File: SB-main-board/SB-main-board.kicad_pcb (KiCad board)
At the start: 4 copper layers, 53 x 40 mm, 98 parts, among them J1 XT30PB_IN, J2 USB_C_Receptacle_USB2.0_16P, J3 Excluder, J4 PT100, J5 Hotend, J6 FAN2, J7 LDC, J8 FS, J9 FAN, Q1 BUK9M8R5-40EX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

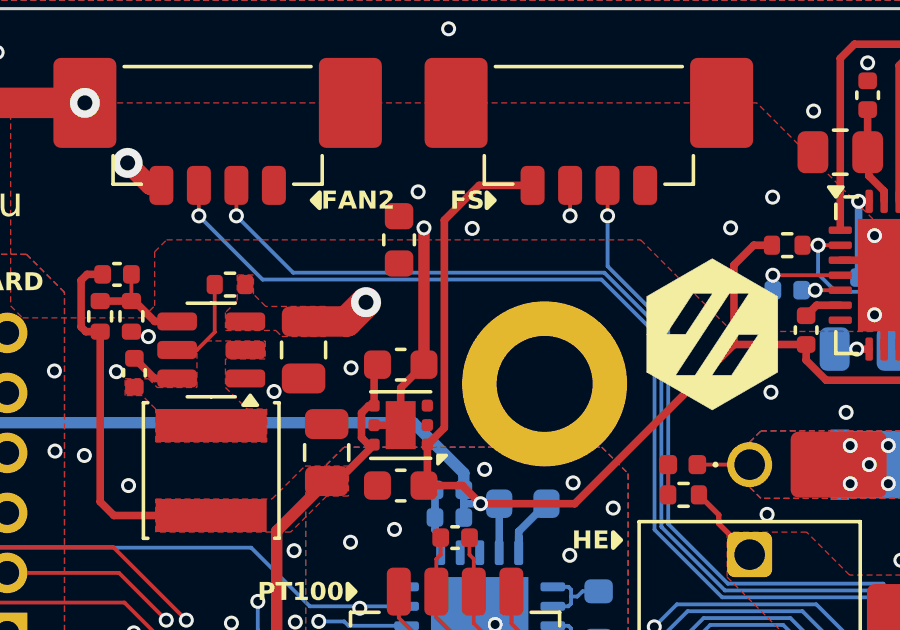
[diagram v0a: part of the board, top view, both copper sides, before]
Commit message: silkscreen: make silkscreen easy to read
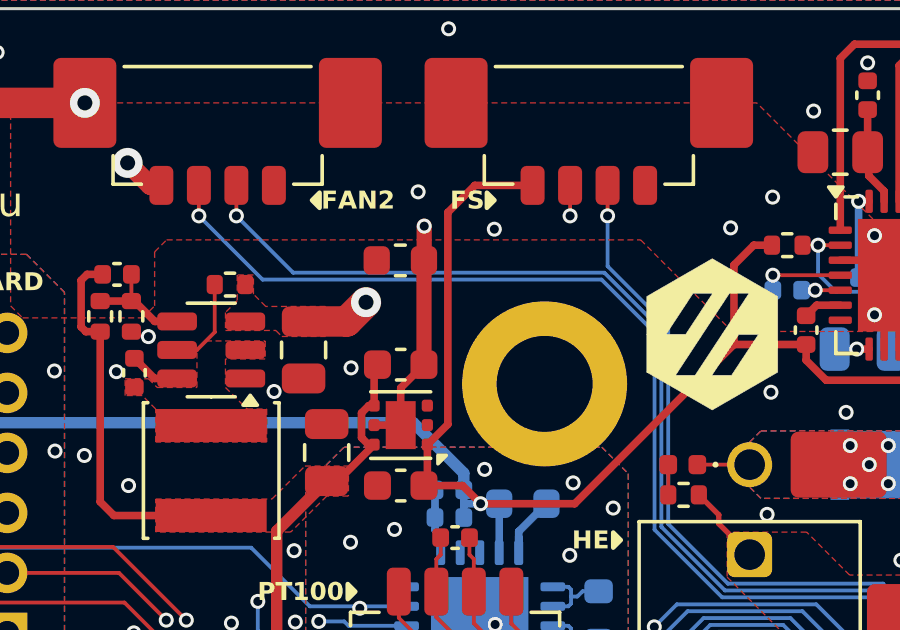
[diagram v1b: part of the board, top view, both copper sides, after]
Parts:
- moved FB4 0.69 mm to (93.3, 76.0), turned to 180 degrees
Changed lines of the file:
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@@
 	(footprint "Inductor_SMD:L_0603_1608Metric"
 		(layer "F.Cu")
-		(at 93.21893 75.305064 -90)
+		(at 93.261329 75.990864 180)
 		(descr "Inductor SMD 0603 (1608 Metric), square (rectangular) end terminal, IPC_7351 nominal, (Body size source: http://www.tortai-tech.com/upload/download/2011102023233369053.pdf), generated with kicad-footprint-generator")
 		(tags "inductor")
 		(property "Reference" "FB4"
-			(at 0 -1.43 90)
+			(at 0 -1.43 360)
 			(layer "F.SilkS")
 			(hide yes)
@@
 		)
 		(property "Value" "120R@100MHz"
-			(at 0 1.43 90)
+			(at 0 1.43 360)
 			(layer "F.Fab")
 			(hide yes)
@@
 		)
 		(property "Footprint" "Inductor_SMD:L_0603_1608Metric"
-			(at 0 0 -90)
+			(at 0 0 180)
 			(unlocked yes)
 			(layer "F.Fab")
@@
 		)
 		(property "Datasheet" ""
-			(at 0 0 -90)
+			(at 0 0 180)
 			(unlocked yes)
 			(layer "F.Fab")
@@
 		)
 		(property "Description" "Ferrite bead"
-			(at 0 0 -90)
+			(at 0 0 180)
 			(unlocked yes)
 			(layer "F.Fab")
@@
 		)
 		(fp_line
-			(start -1.48 0.73)
-			(end -1.48 -0.73)
+			(start 1.48 0.73)
+			(end -1.48 0.73)
 			(stroke
 				(width 0.05)
@@
 		)
 		(fp_line
-			(start 1.48 0.73)
-			(end -1.48 0.73)
+			(start 1.48 -0.73)
+			(end 1.48 0.73)
 			(stroke
 				(width 0.05)
@@
 		)
 		(fp_line
-			(start -1.48 -0.73)
-			(end 1.48 -0.73)
+			(start -1.48 0.73)
+			(end -1.48 -0.73)
 			(stroke
 				(width 0.05)
@@
 		)
 		(fp_line
-			(start 1.48 -0.73)
-			(end 1.48 0.73)
+			(start -1.48 -0.73)
+			(end 1.48 -0.73)
 			(stroke
 				(width 0.05)
@@
 		)
 		(fp_line
-			(start -0.8 0.4)
-			(end -0.8 -0.4)
+			(start 0.8 0.4)
+			(end -0.8 0.4)
 			(stroke
 				(width 0.1)
@@
 		)
 		(fp_line
-			(start 0.8 0.4)
-			(end -0.8 0.4)
+			(start 0.8 -0.4)
+			(end 0.8 0.4)
 			(stroke
 				(width 0.1)
@@
 		)
 		(fp_line
-			(start -0.8 -0.4)
-			(end 0.8 -0.4)
+			(start -0.8 0.4)
+			(end -0.8 -0.4)
 			(stroke
 				(width 0.1)
@@
 		)
 		(fp_line
-			(start 0.8 -0.4)
-			(end 0.8 0.4)
+			(start -0.8 -0.4)
+			(end 0.8 -0.4)
 			(stroke
 				(width 0.1)
@@
 		)
 		(fp_text user "${REFERENCE}"
-			(at 0 0 90)
+			(at 0 0 360)
 			(layer "F.Fab")
 			(effects
@@
 		)
 		(pad "1" smd roundrect
-			(at -0.787501 0 270)
+			(at -0.787501 0 180)
 			(size 0.875 0.95)
 			(layers "F.Cu" "F.Paste" "F.Mask")
@@
 		)
 		(pad "2" smd roundrect
-			(at 0.787501 0 270)
+			(at 0.787501 0 180)
 			(size 0.875 0.95)
 			(layers "F.Cu" "F.Paste" "F.Mask")
@@
 		)
 		(height 4.487268)
-		(gr_text "40.0000 mm"
+		(gr_text "1574.8031 mils"
 			(at 127.27033 87.598664 90)
 			(layer "F.Fab")
@@
 		)
 		(height -3.126866)
-		(gr_text "53.0000 mm"
+		(gr_text "2086.6139 mils"
 			(at 98.906924 64.795664 0)
 			(layer "F.Fab")
@@
 	)
 	(segment
+		(start 94.05713 75.982564)
+		(end 94.04883 75.990864)
+		(width 0.381)
+		(layer "F.Cu")
+		(net 2)
+	)
+	(segment
+		(start 94.04883 74.856164)
+		(end 94.05713 74.847864)
+		(width 0.381)
+		(layer "F.Cu")
+		(net 2)
+	)
+	(segment
 		(start 111.387722 78.946165)
 		(end 111.387722 77.483665)
@@
 	)
 	(segment
-		(start 94.04883 74.905664)
-		(end 94.04883 79.465664)
-		(width 0.381)
+		(start 94.05713 74.847864)
+		(end 94.05713 75.982564)
+		(width 0.508)
 		(layer "F.Cu")
 		(net 2)
@@
 	)
 	(segment
+		(start 94.04883 79.465664)
+		(end 94.04883 75.990864)
+		(width 0.508)
+		(layer "F.Cu")
+		(net 2)
+	)
+	(segment
 		(start 109.887722 75.983665)
 		(end 110.387722 76.483665)
@@
 	)
 	(via
-		(at 95.65733 74.924064)
+		(at 96.39393 74.949464)
 		(size 0.5)
 		(drill 0.3)
@@
 	)
 	(via
-		(at 94.04883 74.905664)
+		(at 94.05713 74.847864)
 		(size 0.5)
 		(drill 0.3)
@@
 	)
 	(segment
-		(start 94.16133 82.130664)
-		(end 94.1698 82.130664)
+		(start 94.84453 81.455934)
+		(end 94.84453 74.390664)
 		(width 0.254)
 		(layer "F.Cu")
@@
 	)
 	(segment
-		(start 94.72743 74.648564)
-		(end 95.88633 73.489664)
+		(start 94.16133 82.130664)
+		(end 94.1698 82.130664)
 		(width 0.254)
 		(layer "F.Cu")
@@
 	)
 	(segment
-		(start 94.72743 81.573034)
-		(end 94.72743 74.648564)
+		(start 106.787722 78.793664)
+		(end 106.787722 79.317056)
 		(width 0.254)
 		(layer "F.Cu")
@@
 	)
 	(segment
-		(start 106.787722 78.793664)
-		(end 106.787722 79.317056)
+		(start 95.74553 73.489664)
+		(end 97.66933 73.489664)
 		(width 0.254)
 		(layer "F.Cu")
@@
 	)
 	(segment
+		(start 94.1698 82.130664)
+		(end 94.84453 81.455934)
+		(width 0.254)
+		(layer "F.Cu")
+		(net 99)
+	)
+	(segment
 		(start 105.042329 75.483665)
 		(end 104.38233 76.143664)
@@
 	)
 	(segment
-		(start 95.88633 73.489664)
-		(end 97.66933 73.489664)
+		(start 94.84453 74.390664)
+		(end 95.74553 73.489664)
 		(width 0.254)
 		(layer "F.Cu")
@@
 		(width 0.254)
 		(layer "F.Cu")
-		(net 99)
-	)
-	(segment
-		(start 94.1698 82.130664)
-		(end 94.72743 81.573034)
-		(width 0.254)
-		(layer "F.Cu")

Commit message: layout: optmise power layout
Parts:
- added FB6: 120R@100MHz, Inductor_SMD:L_0603_1608Metric, B.Cu at (100.9, 85.3)
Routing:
- net /SPI0_CS2: track 42.5 -> 41.6 mm
- net /FAN1_DET: track 55.1 -> 54.3 mm
- net /FAN0_DET: track 52.5 -> 53.1 mm
